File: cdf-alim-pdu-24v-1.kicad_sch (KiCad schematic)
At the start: 123 parts, among them J1 Conn_01x02, J10 Conn_01x02, J11 Conn_01x02, J12 Conn_01x02, J13 Conn_01x02, J14 Conn_01x02, J15 Conn_01x02, J16 Conn_01x02, J17 Conn_01x02, J18 Conn_01x02, J19 Conn_01x02, J3 Conn_01x02, J5 Conn_01x02, J6 Conn_01x02, J7 Conn_01x02, J8 Conn_01x02, J9 Conn_01x02, Q3 BSC019N04LS, Q4 BSC019N04LS, Q5 BSC019N04LS, U1 HT753-1, U2 TPS25983, U3 TPS25983, U4 TPS25983, U5 MX25947, U6 MX25947, U7 MX25947

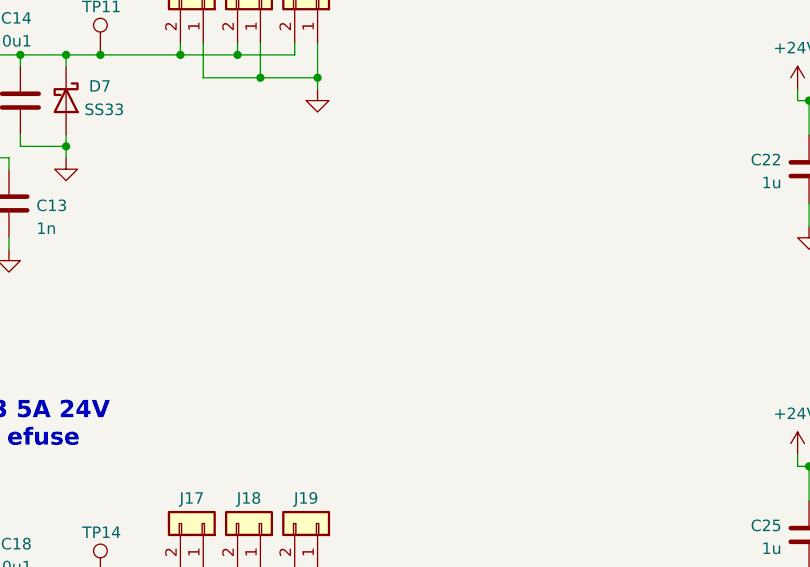
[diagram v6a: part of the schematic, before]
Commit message: schem: add assembly and mounting holes
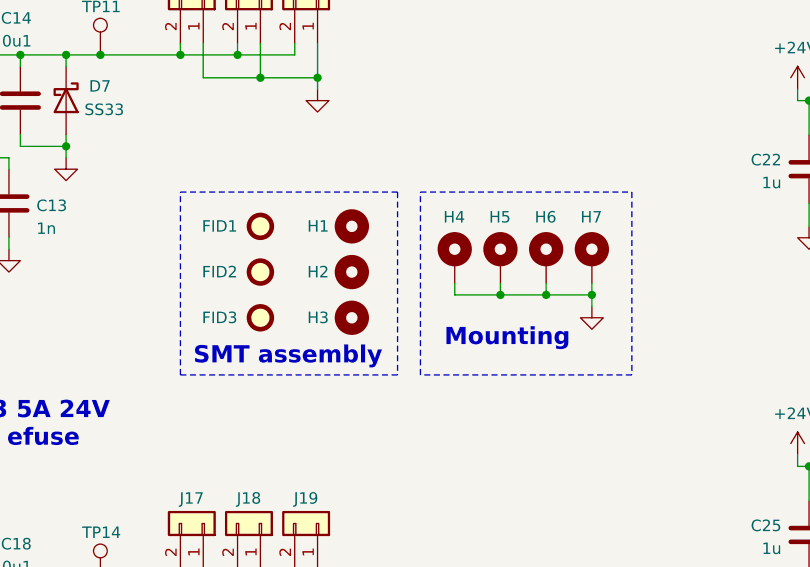
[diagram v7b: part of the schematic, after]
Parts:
- added FID1, FID2, FID3: Fiducial, Fiducial:Fiducial_1mm_Mask2mm, symbol Mechanical:Fiducial
- added H1, H2, H3: MountingHole, MountingHole:ToolingHole_1.152mm, symbol Mechanical:MountingHole
- added H4, H5, H6, H7: MountingHole_Pad, MountingHole:MountingHole_3.2mm_M3_Pad_Via, symbol Mechanical:MountingHole_Pad
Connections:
- net GND: now also H4.1, H5.1, H6.1, H7.1
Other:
- note added: "Mounting"
- note added: "SMT assembly"

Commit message: schem: fix input efuse dvdt
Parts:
- C10: value 1n -> 10n; JLCPCB Part # C1588 -> C57112; Manufacturer Part Number CL10B102KB8NNNC -> 0603B103K500NT
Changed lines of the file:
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@@
 			)
 		)
-		(property "Value" "1n"
+		(property "Value" "10n"
 			(at 104.648 44.704 0)
 			(show_name no)
@@
 			)
 		)
-		(property "JLCPCB Part #" "C1588"
+		(property "JLCPCB Part #" "C57112"
 			(at 101.6 41.91 0)
 			(hide yes)
@@
 			)
 		)
-		(property "Manufacturer Part Number" "CL10B102KB8NNNC"
+		(property "Manufacturer Part Number" "0603B103K500NT"
 			(at 101.6 41.91 0)
 			(hide yes)
